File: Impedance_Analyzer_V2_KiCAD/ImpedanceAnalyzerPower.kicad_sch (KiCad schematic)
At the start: 37 parts, among them J8 Barrel_Jack_Switch, J9 USB_B_Micro, U1 LM358, U5 L7805

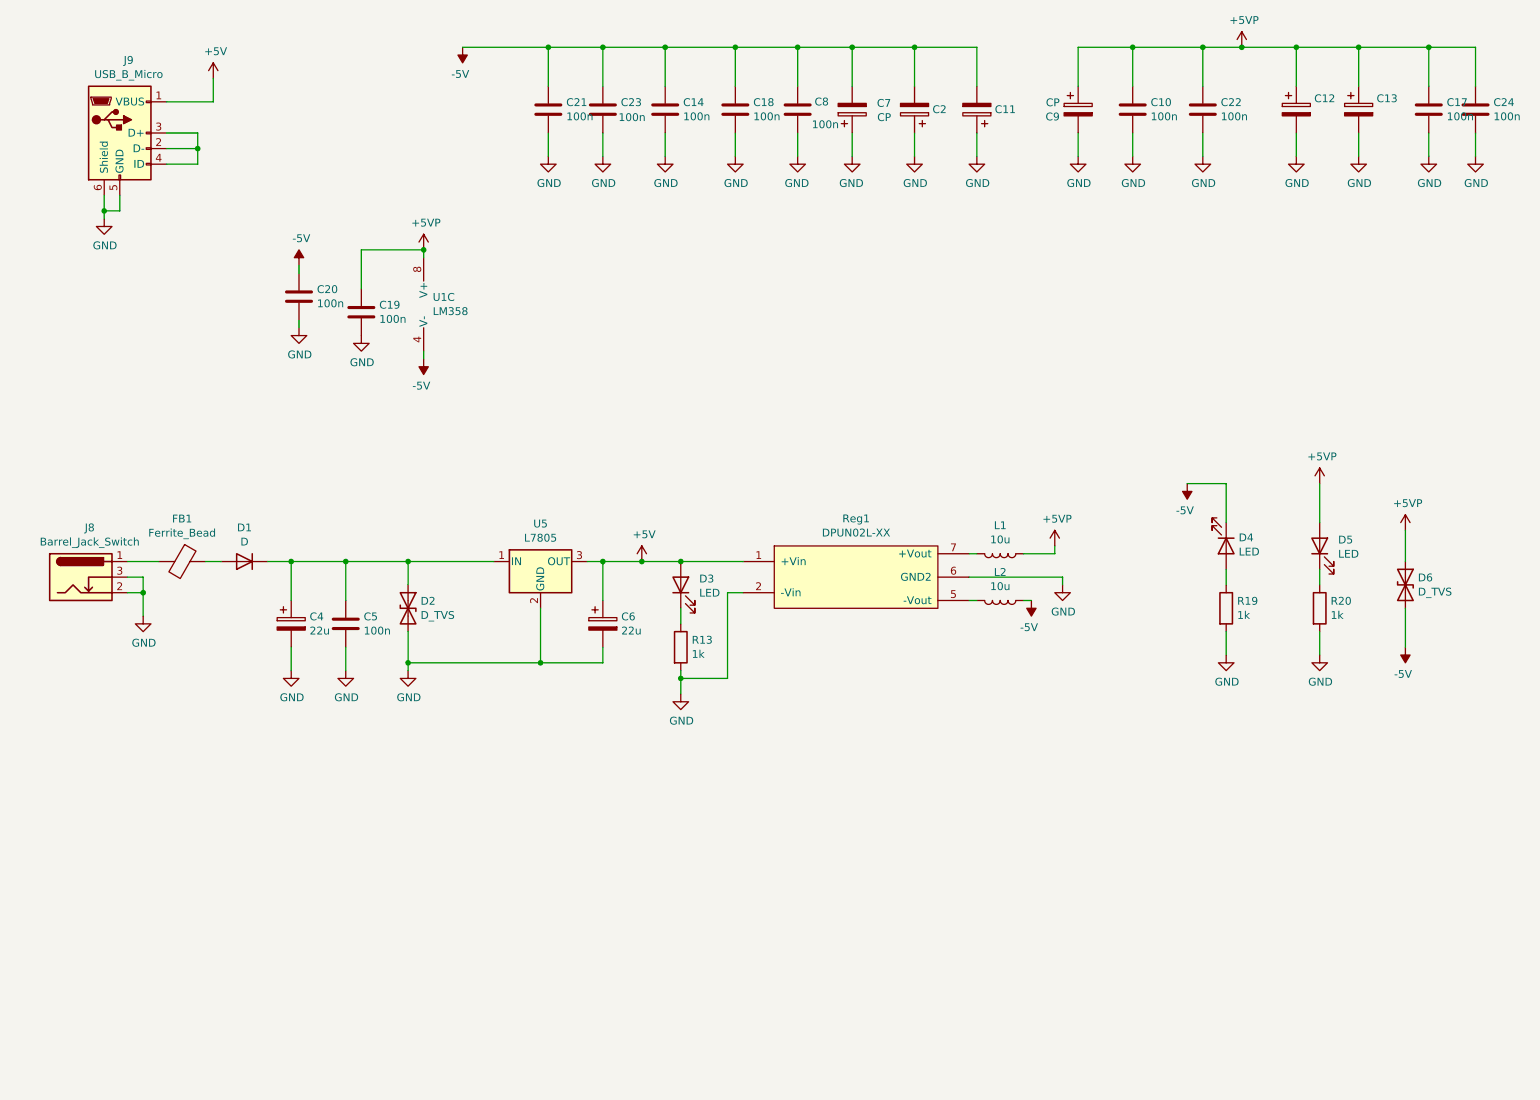
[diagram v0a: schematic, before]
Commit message: Make Rev C + Curve tracer init
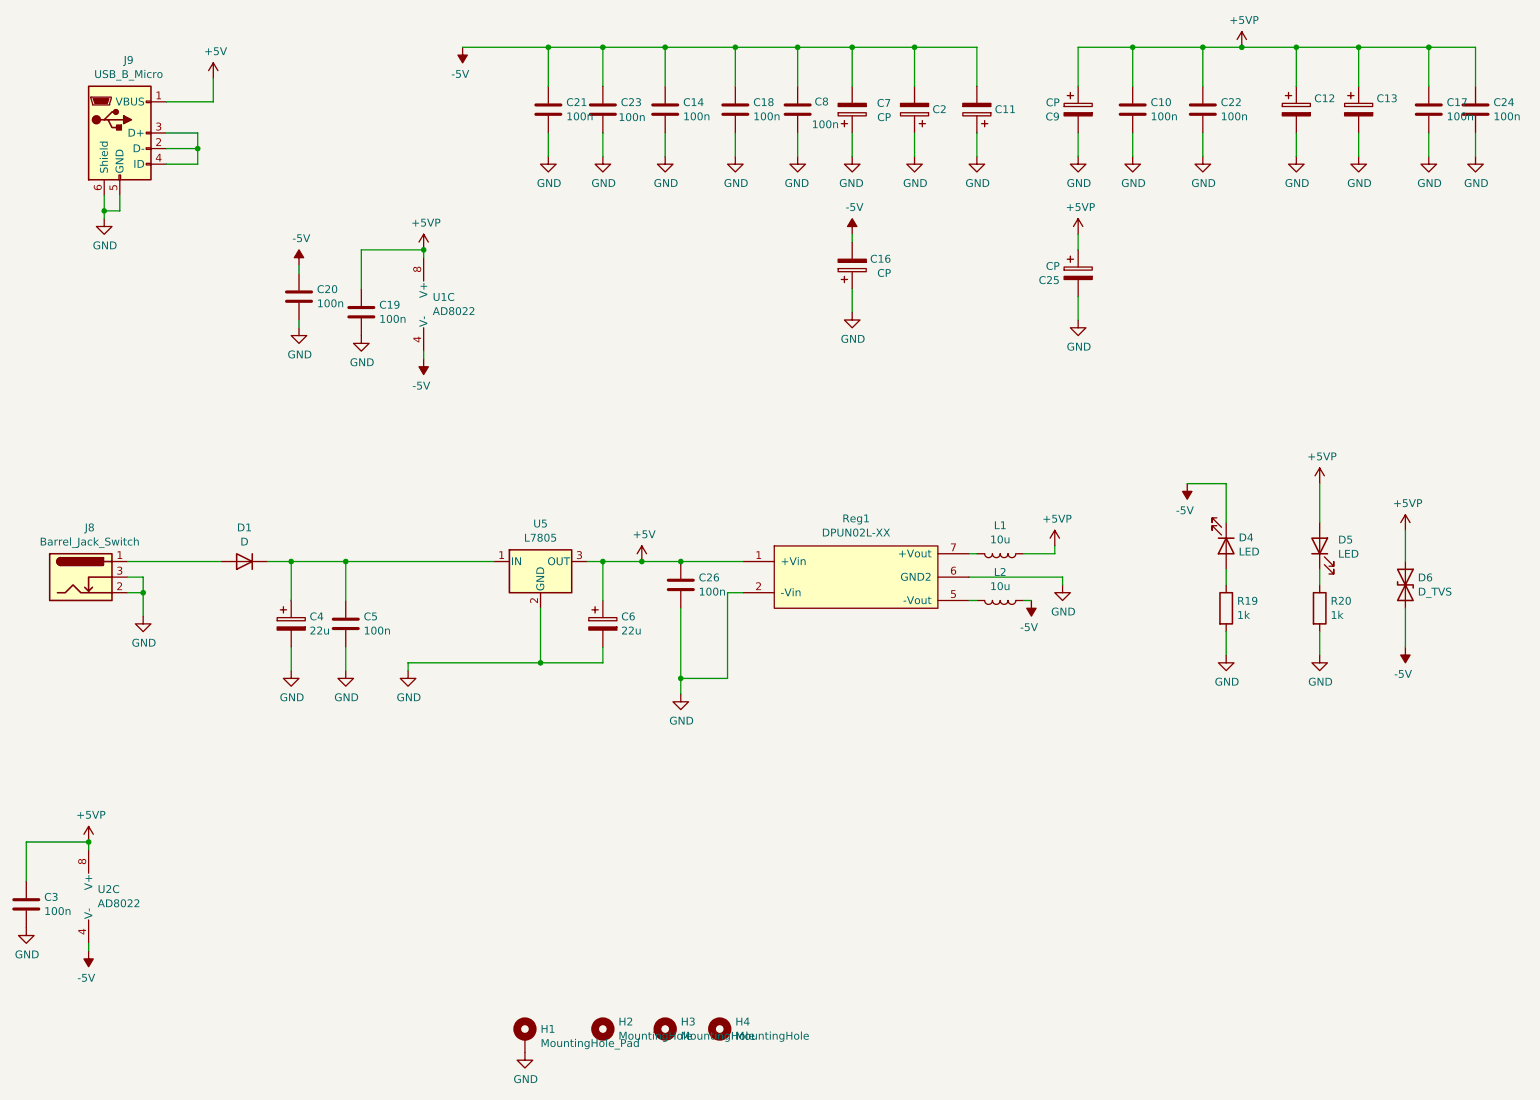
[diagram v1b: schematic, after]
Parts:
- removed D2: D_TVS, Diode_SMD:D_SMA, symbol Device:D_TVS
- removed D3: LED, LED_SMD:LED_1206_3216Metric, symbol Device:LED
- removed FB1: Ferrite_Bead, Resistor_SMD:R_0805_2012Metric, symbol Device:Ferrite_Bead
- removed R13: 1k, Resistor_SMD:R_1206_3216Metric, symbol Device:R
- added C16, C25: CP, Capacitor_THT:CP_Radial_D8.0mm_P5.00mm, symbol Device:CP
- added C26, C3: 100n, Capacitor_SMD:C_0805_2012Metric, symbol Device:C
- added H1: MountingHole_Pad, MountingHole:MountingHole_4.3mm_M4_Pad, symbol Mechanical:MountingHole_Pad
- added H2, H3, H4: MountingHole, MountingHole:MountingHole_4mm, symbol Mechanical:MountingHole
- added U2: AD8022, Package_SO:SO-8_3.9x4.9mm_P1.27mm, symbol Amplifier_Operational:LM358
- U1: value LM358 -> AD8022
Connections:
- net +5V: now also C26.1
- net +5VP: now also C25.1, C3.1, U2.8 (V+)
- net -5V: now also C16.2, U2.4 (V-)
- net GND: now also C16.1, C25.2, C26.2, C3.2, H1.1
- net at J8.1: now also D1.2 (A)
